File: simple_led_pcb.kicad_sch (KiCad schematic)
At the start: 3 parts

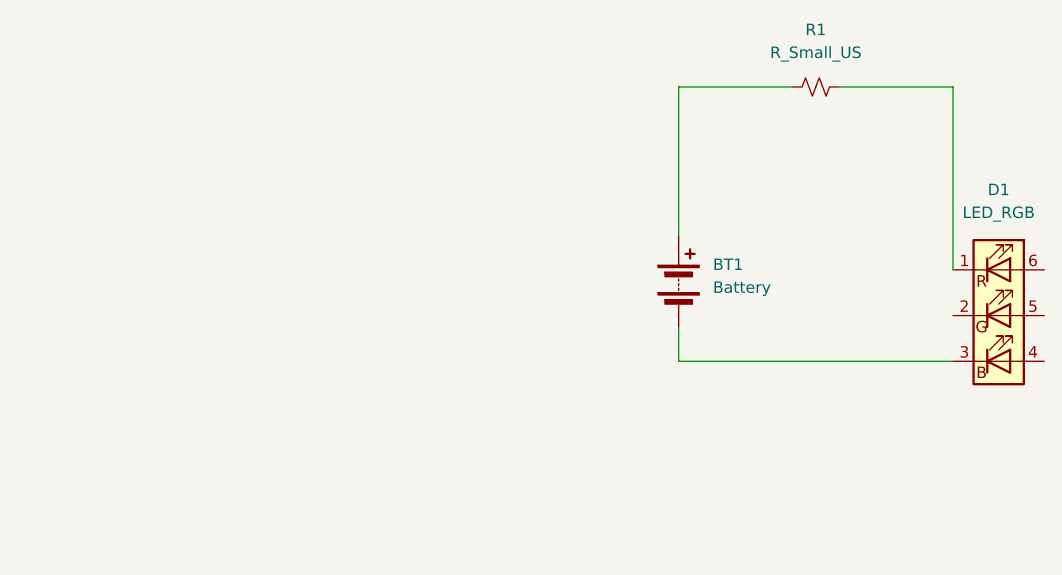
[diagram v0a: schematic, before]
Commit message: add sch for simple led pcb
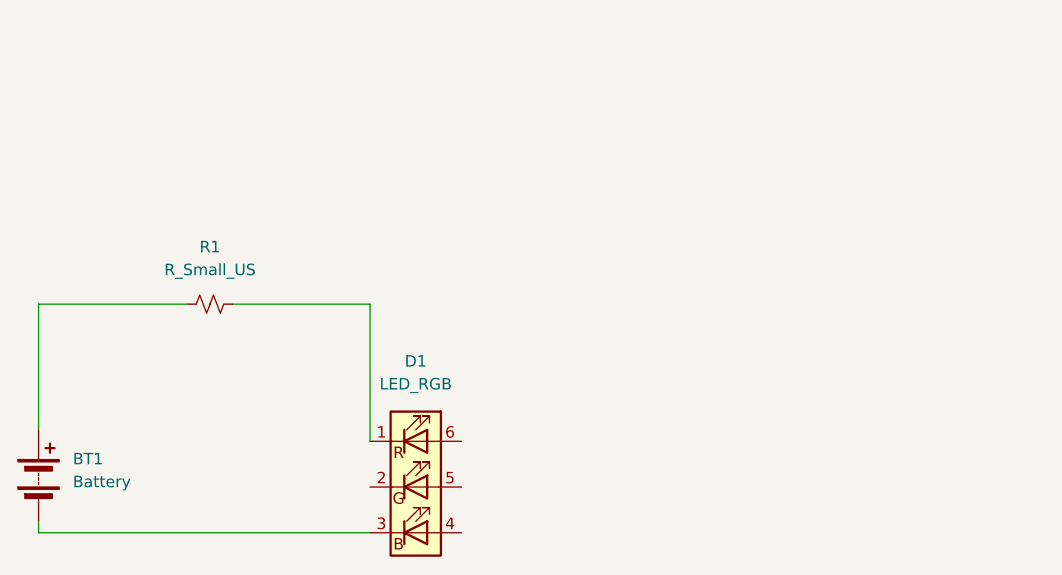
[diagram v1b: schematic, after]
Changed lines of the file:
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@@
 	(wire
 		(pts
-			(xy 152.4 73.66) (xy 182.88 73.66)
-		)
-		(stroke
-			(width 0)
-			(type default)
-		)
-	)
-	(wire
-		(pts
-			(xy 152.4 59.69) (xy 152.4 43.18)
-		)
-		(stroke
-			(width 0)
-			(type default)
-		)
-	)
-	(wire
-		(pts
-			(xy 182.88 43.18) (xy 182.88 63.5)
-		)
-		(stroke
-			(width 0)
-			(type default)
-		)
-	)
-	(wire
-		(pts
-			(xy 152.4 69.85) (xy 152.4 73.66)
-		)
-		(stroke
-			(width 0)
-			(type default)
-		)
-	)
-	(wire
-		(pts
-			(xy 152.4 43.18) (xy 165.1 43.18)
-		)
-		(stroke
-			(width 0)
-			(type default)
-		)
-	)
-	(wire
-		(pts
-			(xy 170.18 43.18) (xy 182.88 43.18)
-		)
-		(stroke
-			(width 0)
-			(type default)
+			(xy 102.87 67.31) (xy 118.11 67.31)
+		)
+		(stroke
+			(width 0)
+			(type default)
+		)
+	)
+	(wire
+		(pts
+			(xy 81.28 92.71) (xy 118.11 92.71)
+		)
+		(stroke
+			(width 0)
+			(type default)
+		)
+	)
+	(wire
+		(pts
+			(xy 118.11 67.31) (xy 118.11 82.55)
+		)
+		(stroke
+			(width 0)
+			(type default)
+		)
+	)
+	(wire
+		(pts
+			(xy 81.28 81.28) (xy 81.28 67.31)
+		)
+		(stroke
+			(width 0)
+			(type default)
+		)
+	)
+	(wire
+		(pts
+			(xy 81.28 91.44) (xy 81.28 92.71)
+		)
+		(stroke
+			(width 0)
+			(type default)
+		)
+	)
+	(wire
+		(pts
+			(xy 81.28 67.31) (xy 97.79 67.31)
+		)
+		(stroke
+			(width 0)
+			(type default)
+		)
+	)
+	(symbol
+		(lib_id "Device:Battery")
+		(at 81.28 86.36 0)
+		(unit 1)
+		(exclude_from_sim no)
+		(in_bom yes)
+		(on_board yes)
+		(dnp no)
+		(fields_autoplaced yes)
+		(property "Reference" "BT1"
+			(at 85.09 84.5184 0)
+			(effects
+				(font
+					(size 1.27 1.27)
+				)
+				(justify left)
+			)
+		)
+		(property "Value" "Battery"
+			(at 85.09 87.0584 0)
+			(effects
+				(font
+					(size 1.27 1.27)
+				)
+				(justify left)
+			)
+		)
+		(property "Footprint" ""
+			(at 81.28 84.836 90)
+			(effects
+				(font
+					(size 1.27 1.27)
+				)
+				(hide yes)
+			)
+		)
+		(property "Datasheet" "~"
+			(at 81.28 84.836 90)
+			(effects
+				(font
+					(size 1.27 1.27)
+				)
+				(hide yes)
+			)
+		)
+		(property "Description" "Multiple-cell battery"
+			(at 81.28 86.36 0)
+			(effects
+				(font
+					(size 1.27 1.27)
+				)
+				(hide yes)
+			)
+		)
+		(pin "2"
+		)
+		(pin "1"
+		)
+		(instances
+			(project ""
+				(path "/a6f41b6e-59ed-4005-bac5-fbb3811063d2"
+					(reference "BT1")
+					(unit 1)
+				)
+			)
+		)
+	)
+	(symbol
+		(lib_id "Device:R_Small_US")
+		(at 100.33 67.31 90)
+		(unit 1)
+		(exclude_from_sim no)
+		(in_bom yes)
+		(on_board yes)
+		(dnp no)
+		(fields_autoplaced yes)
+		(property "Reference" "R1"
+			(at 100.33 60.96 90)
+			(effects
+				(font
+					(size 1.27 1.27)
+				)
+			)
+		)
+		(property "Value" "R_Small_US"
+			(at 100.33 63.5 90)
+			(effects
+				(font
+					(size 1.27 1.27)
+				)
+			)
+		)
+		(property "Footprint" ""
+			(at 100.33 67.31 0)
+			(effects
+				(font
+					(size 1.27 1.27)
+				)
+				(hide yes)
+			)
+		)
+		(property "Datasheet" "~"
+			(at 100.33 67.31 0)
+			(effects
+				(font
+					(size 1.27 1.27)
+				)
+				(hide yes)
+			)
+		)
+		(property "Description" "Resistor, small US symbol"
+			(at 100.33 67.31 0)
+			(effects
+				(font
+					(size 1.27 1.27)
+				)
+				(hide yes)
+			)
+		)
+		(pin "2"
+		)
+		(pin "1"
+		)
+		(instances
+			(project ""
+				(path "/a6f41b6e-59ed-4005-bac5-fbb3811063d2"
+					(reference "R1")
+					(unit 1)
+				)
+			)
 		)
 	)
 	(symbol
 		(lib_id "Device:LED_RGB")
-		(at 187.96 68.58 0)
+		(at 123.19 87.63 0)
 		(unit 1)
 		(exclude_from_sim no)
@@
 		(fields_autoplaced yes)
 		(property "Reference" "D1"
-			(at 187.96 54.61 0)
+			(at 123.19 73.66 0)
 			(effects
 				(font
@@
 		)
 		(property "Value" "LED_RGB"
-			(at 187.96 57.15 0)
+			(at 123.19 76.2 0)
 			(effects
 				(font
@@
 		)
 		(property "Footprint" ""
-			(at 187.96 69.85 0)
+			(at 123.19 88.9 0)
 			(effects
 				(font
@@
 		)
 		(property "Datasheet" "~"
-			(at 187.96 69.85 0)
+			(at 123.19 88.9 0)
 			(effects
 				(font
@@
 		)
 		(property "Description" "RGB LED, 6 pin package"
-			(at 187.96 68.58 0)
+			(at 123.19 87.63 0)
 			(effects
 				(font
@@
 		(pin "1"
 		)
+		(pin "6"
+		)
+		(pin "4"
+		)
+		(pin "5"
+		)
 		(pin "3"
-		)
-		(pin "6"
-		)
-		(pin "5"
-		)
-		(pin "4"
 		)
 		(instances
 			(project ""
-				(path "/601757d4-64e8-4710-bf76-b4024de1bea3"
+				(path "/a6f41b6e-59ed-4005-bac5-fbb3811063d2"
 					(reference "D1")
 					(unit 1)
 				)
-			)
-		)
-	)
-	(symbol
-		(lib_id "Device:Battery")
-		(at 152.4 64.77 0)
-		(unit 1)
-		(exclude_from_sim no)
-		(in_bom yes)
-		(on_board yes)
-		(dnp no)
-		(fields_autoplaced yes)
-		(property "Reference" "BT1"
-			(at 156.21 62.9284 0)
-			(effects
-				(font
-					(size 1.27 1.27)
-				)
-				(justify left)
-			)
-		)
-		(property "Value" "Battery"
-			(at 156.21 65.4684 0)
-			(effects
-				(font
-					(size 1.27 1.27)
-				)
-				(justify left)
-			)
-		)
-		(property "Footprint" ""
-			(at 152.4 63.246 90)
-			(effects
-				(font
-					(size 1.27 1.27)
-				)
-				(hide yes)
-			)
-		)
-		(property "Datasheet" "~"
-			(at 152.4 63.246 90)
-			(effects
-				(font
-					(size 1.27 1.27)
-				)
-				(hide yes)
-			)
-		)
-		(property "Description" "Multiple-cell battery"
-			(at 152.4 64.77 0)
-			(effects
-				(font
-					(size 1.27 1.27)
-				)
-				(hide yes)
-			)
-		)
-		(pin "2"
-		)
-		(pin "1"
-		)
-		(instances
-			(project ""
-				(path "/601757d4-64e8-4710-bf76-b4024de1bea3"
-					(reference "BT1")
-					(unit 1)
-				)
-			)
-		)
-	)
-	(symbol
-		(lib_id "Device:R_Small_US")
-		(at 167.64 43.18 90)
-		(unit 1)
-		(exclude_from_sim no)
-		(in_bom yes)
-		(on_board yes)
-		(dnp no)
-		(fields_autoplaced yes)
-		(property "Reference" "R1"
-			(at 167.64 36.83 90)
-			(effects
-				(font
-					(size 1.27 1.27)
-				)
-			)
-		)
-		(property "Value" "R_Small_US"
-			(at 167.64 39.37 90)
-			(effects
-				(font
-					(size 1.27 1.27)
-				)
-			)
-		)
-		(property "Footprint" ""
-			(at 167.64 43.18 0)
-			(effects
-				(font
-					(size 1.27 1.27)
-				)
-				(hide yes)
-			)
-		)
-		(property "Datasheet" "~"
-			(at 167.64 43.18 0)
-			(effects
-				(font
-					(size 1.27 1.27)
-				)
-				(hide yes)
-			)
-		)
-		(property "Description" "Resistor, small US symbol"
-			(at 167.64 43.18 0)
-			(effects
-				(font
-					(size 1.27 1.27)
-				)
-				(hide yes)
-			)
-		)
-		(pin "2"
-		)
-		(pin "1"
-		)
-		(instances
-			(project ""
-				(path "/601757d4-64e8-4710-bf76-b4024de1bea3"
-					(reference "R1")
-					(unit 1)
-				)

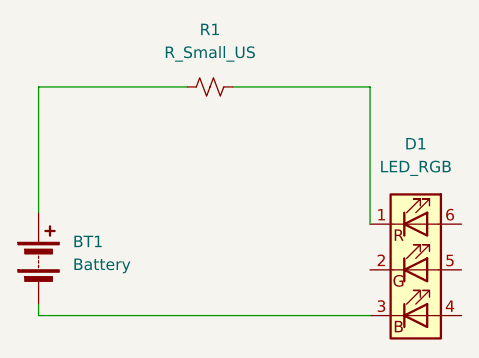
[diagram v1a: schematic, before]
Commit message: update R1 name and R to LED trace
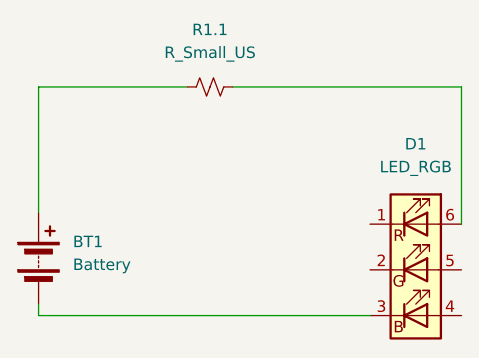
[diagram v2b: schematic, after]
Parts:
- renumbered R1 to R1.1
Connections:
- net at R1.1.2: now also D1.6 (RA); no longer D1.1 (RK)
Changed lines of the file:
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@@
 	(wire
 		(pts
-			(xy 102.87 67.31) (xy 118.11 67.31)
+			(xy 102.87 67.31) (xy 128.27 67.31)
 		)
 		(stroke
@@
 		(pts
 			(xy 81.28 92.71) (xy 118.11 92.71)
-		)
-		(stroke
-			(width 0)
-			(type default)
-		)
-	)
-	(wire
-		(pts
-			(xy 118.11 67.31) (xy 118.11 82.55)
 		)
 		(stroke
@@
 		(pts
 			(xy 81.28 67.31) (xy 97.79 67.31)
+		)
+		(stroke
+			(width 0)
+			(type default)
+		)
+	)
+	(wire
+		(pts
+			(xy 128.27 67.31) (xy 128.27 82.55)
 		)
 		(stroke
@@
 		(dnp no)
 		(fields_autoplaced yes)
-		(property "Reference" "R1"
+		(property "Reference" "R1.1"
 			(at 100.33 60.96 90)
 			(effects
@@
 			(project ""
 				(path "/a6f41b6e-59ed-4005-bac5-fbb3811063d2"
-					(reference "R1")
+					(reference "R1.1")
 					(unit 1)
 				)
